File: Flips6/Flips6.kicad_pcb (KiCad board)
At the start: 2 copper layers, 100 x 50 mm, 25 parts, among them CN1 Conn_02x04_Odd_Even, IC1 74595, IC2 74595, IC3 74595

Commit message: moving abandoned project, renaming remaining
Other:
- board text added: "SRT Flips 6 V1.0 2018-11-15 github.com/cawapy/FlipSuite"
- board text removed: "SRT Flips 6c V1.0 2018-11-15 github.com/cawapy/FlipSuite"
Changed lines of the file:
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@@
   (gr_line (start 230.505 78.105) (end 239.395 78.105) (layer F.SilkS) (width 0.1))
   (gr_line (start 240.665 78.105) (end 249.555 78.105) (layer F.SilkS) (width 0.1))
-  (gr_text "SRT Flips 6c V1.0 2018-11-15\ngithub.com/cawapy/FlipSuite" (at 190.5 104.775) (layer F.SilkS)
+  (gr_text "SRT Flips 6 V1.0 2018-11-15\ngithub.com/cawapy/FlipSuite" (at 190.5 104.775) (layer F.SilkS)
     (effects (font (size 1.5 1.5) (thickness 0.3)) (justify left))
   )

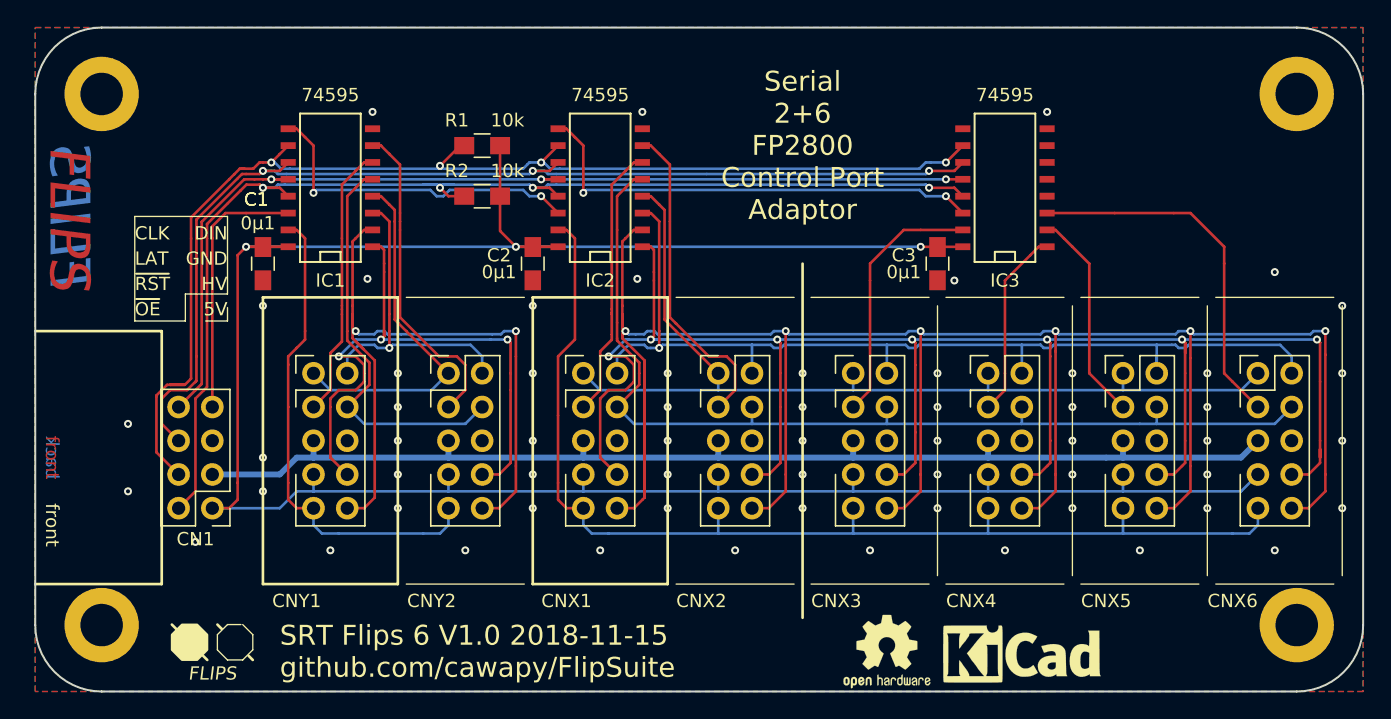
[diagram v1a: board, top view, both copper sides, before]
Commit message: adjust titles and labels
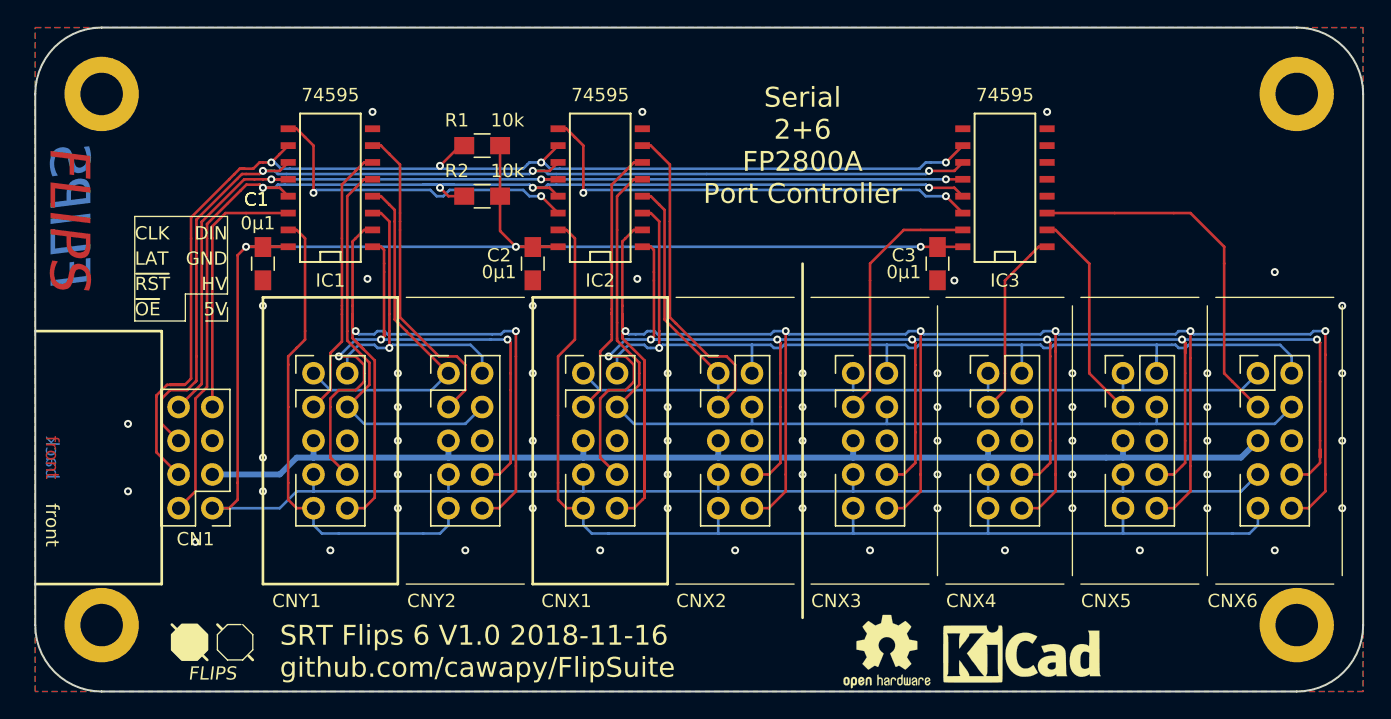
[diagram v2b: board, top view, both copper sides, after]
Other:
- board text added: "SRT Flips 6 V1.0 2018-11-16 github.com/cawapy/FlipSuite"
- board text added: "Serial 2+6 FP2800A Port Controller"
- board text removed: "SRT Flips 6 V1.0 2018-11-15 github.com/cawapy/FlipSuite"
- board text removed: "Serial 2+6 FP2800 Control Port Adaptor"
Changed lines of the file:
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@@
     (effects (font (size 1 1) (thickness 0.15)) (justify left))
   )
-  (gr_text "Serial\n2+6\nFP2800\nControl Port\nAdaptor" (at 229.87 66.675) (layer F.SilkS)
+  (gr_text "Serial\n2+6\nFP2800A\nPort Controller" (at 229.87 66.675) (layer F.SilkS)
     (effects (font (size 1.5 1.5) (thickness 0.3)))
   )
@@
   (gr_line (start 230.505 78.105) (end 239.395 78.105) (layer F.SilkS) (width 0.1))
   (gr_line (start 240.665 78.105) (end 249.555 78.105) (layer F.SilkS) (width 0.1))
-  (gr_text "SRT Flips 6 V1.0 2018-11-15\ngithub.com/cawapy/FlipSuite" (at 190.5 104.775) (layer F.SilkS)
+  (gr_text "SRT Flips 6 V1.0 2018-11-16\ngithub.com/cawapy/FlipSuite" (at 190.5 104.775) (layer F.SilkS)
     (effects (font (size 1.5 1.5) (thickness 0.3)) (justify left))
   )
